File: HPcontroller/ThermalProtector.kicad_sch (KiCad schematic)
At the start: 5 parts

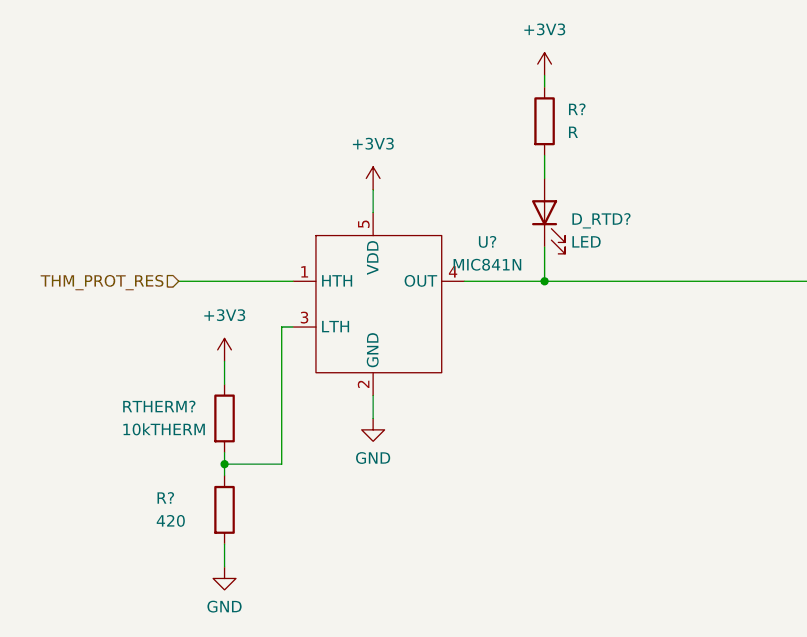
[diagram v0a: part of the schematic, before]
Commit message: assigned footprints, added some stuff to readme
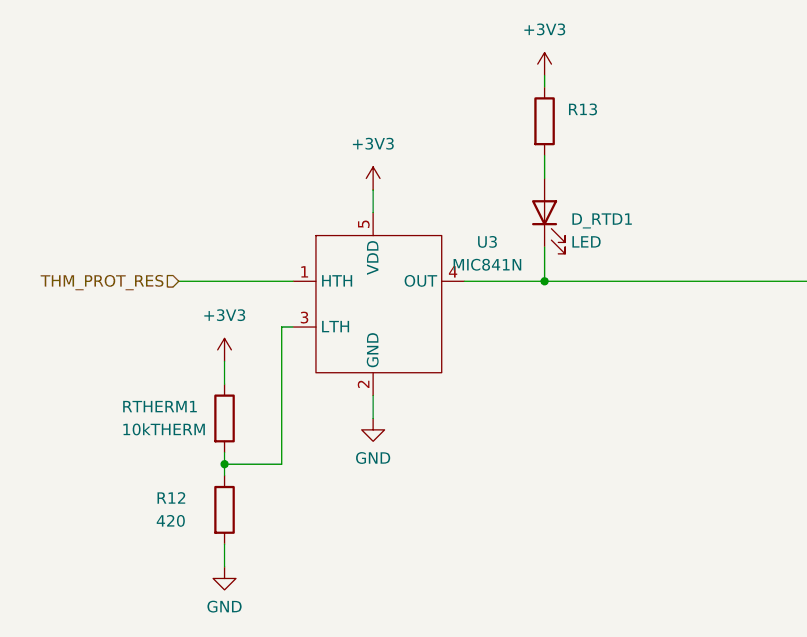
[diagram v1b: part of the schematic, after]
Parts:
- R13: renamed from R?; value R -> (none)
- gave numbers to parts that had none: 4
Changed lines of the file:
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@@
   (symbol (lib_id "Device:R") (at 114.3 104.14 0) (unit 1)
     (in_bom yes) (on_board yes)
-    (property "Reference" "RTHERM?" (id 0) (at 102.87 102.87 0)
+    (property "Reference" "RTHERM1" (id 0) (at 102.87 102.87 0)
       (effects (font (size 1.27 1.27)) (justify left))
     )
@@
   (symbol (lib_id "power:+3V3") (at 149.86 66.04 0) (unit 1)
     (in_bom yes) (on_board yes) (fields_autoplaced)
-    (property "Reference" "#PWR?" (id 0) (at 149.86 69.85 0)
+    (property "Reference" "#PWR0117" (id 0) (at 149.86 69.85 0)
       (effects (font (size 1.27 1.27)) hide)
     )
@@
   (symbol (lib_id "Device:R") (at 149.86 71.12 0) (unit 1)
     (in_bom yes) (on_board yes) (fields_autoplaced)
-    (property "Reference" "R?" (id 0) (at 152.4 69.8499 0)
+    (property "Reference" "R13" (id 0) (at 152.4 69.8499 0)
       (effects (font (size 1.27 1.27)) (justify left))
     )
-    (property "Value" "R" (id 1) (at 152.4 72.3899 0)
+    (property "Value" "" (id 1) (at 152.4 72.3899 0)
       (effects (font (size 1.27 1.27)) (justify left))
     )
@@
   (symbol (lib_id "Device:LED") (at 149.86 81.28 90) (unit 1)
     (in_bom yes) (on_board yes) (fields_autoplaced)
-    (property "Reference" "D_RTD?" (id 0) (at 152.781 82.0328 90)
+    (property "Reference" "D_RTD1" (id 0) (at 152.781 82.0328 90)
       (effects (font (size 1.27 1.27)) (justify right))
     )
@@
   (symbol (lib_id "power:+3V3") (at 114.3 97.79 0) (unit 1)
     (in_bom yes) (on_board yes) (fields_autoplaced)
-    (property "Reference" "#PWR?" (id 0) (at 114.3 101.6 0)
+    (property "Reference" "#PWR0115" (id 0) (at 114.3 101.6 0)
       (effects (font (size 1.27 1.27)) hide)
     )
@@
   (symbol (lib_id "power:GND") (at 130.81 104.14 0) (unit 1)
     (in_bom yes) (on_board yes) (fields_autoplaced)
-    (property "Reference" "#PWR?" (id 0) (at 130.81 110.49 0)
+    (property "Reference" "#PWR0118" (id 0) (at 130.81 110.49 0)
       (effects (font (size 1.27 1.27)) hide)
     )
@@
   (symbol (lib_id "power:GND") (at 114.3 120.65 0) (unit 1)
     (in_bom yes) (on_board yes) (fields_autoplaced)
-    (property "Reference" "#PWR?" (id 0) (at 114.3 127 0)
+    (property "Reference" "#PWR0114" (id 0) (at 114.3 127 0)
       (effects (font (size 1.27 1.27)) hide)
     )
@@
   (symbol (lib_id "HPsym:MIC841N") (at 130.81 91.44 0) (unit 1)
     (in_bom yes) (on_board yes) (fields_autoplaced)
-    (property "Reference" "U?" (id 0) (at 143.51 84.5693 0))
+    (property "Reference" "U3" (id 0) (at 143.51 84.5693 0))
     (property "Value" "MIC841N" (id 1) (at 143.51 87.1093 0))
     (property "Footprint" "" (id 2) (at 121.92 88.9 0)
@@
   (symbol (lib_id "power:+3V3") (at 130.81 78.74 0) (unit 1)
     (in_bom yes) (on_board yes) (fields_autoplaced)
-    (property "Reference" "#PWR?" (id 0) (at 130.81 82.55 0)
+    (property "Reference" "#PWR0116" (id 0) (at 130.81 82.55 0)
       (effects (font (size 1.27 1.27)) hide)
     )
@@
   (symbol (lib_id "Device:R") (at 114.3 114.3 0) (unit 1)
     (in_bom yes) (on_board yes)
-    (property "Reference" "R?" (id 0) (at 106.68 113.03 0)
+    (property "Reference" "R12" (id 0) (at 106.68 113.03 0)
       (effects (font (size 1.27 1.27)) (justify left))
     )

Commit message: started layout
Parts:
- added C5: C, symbol Device:C
- D_RTD1: footprint (none) -> LED_SMD:LED_0603_1608Metric_Pad1.05x0.95mm_HandSolder
- R12: footprint (none) -> Resistor_SMD:R_0805_2012Metric_Pad1.20x1.40mm_HandSolder
- R13: value (none) -> 100; footprint (none) -> Resistor_SMD:R_0805_2012Metric_Pad1.20x1.40mm_HandSolder
- U3: footprint (none) -> Package_TO_SOT_SMD:SOT-353_SC-70-5_Handsoldering
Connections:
- net +3V3: now also C5.1
- net GND: now also C5.2
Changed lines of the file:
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@@
   (junction (at 114.3 109.22) (diameter 0) (color 0 0 0 0)
   )
+  (junction (at 130.81 71.12) (diameter 0) (color 0 0 0 0)
+  )
   (wire (pts (xy 149.86 88.9) (xy 185.42 88.9))
     (stroke (width 0) (type default) (color 0 0 0 0))
@@
     (stroke (width 0) (type default) (color 0 0 0 0))
   )
+  (wire (pts (xy 116.84 73.66) (xy 116.84 71.12))
+    (stroke (width 0) (type default) (color 0 0 0 0))
+  )
   (wire (pts (xy 114.3 109.22) (xy 114.3 110.49))
     (stroke (width 0) (type default) (color 0 0 0 0))
@@
     (stroke (width 0) (type default) (color 0 0 0 0))
   )
-  (wire (pts (xy 130.81 78.74) (xy 130.81 81.28))
+  (wire (pts (xy 130.81 68.58) (xy 130.81 71.12))
     (stroke (width 0) (type default) (color 0 0 0 0))
   )
@@
     (stroke (width 0) (type default) (color 0 0 0 0))
   )
+  (wire (pts (xy 116.84 82.55) (xy 116.84 81.28))
+    (stroke (width 0) (type default) (color 0 0 0 0))
+  )
   (wire (pts (xy 149.86 88.9) (xy 140.97 88.9))
     (stroke (width 0) (type default) (color 0 0 0 0))
@@
     (stroke (width 0) (type default) (color 0 0 0 0))
   )
+  (wire (pts (xy 116.84 71.12) (xy 130.81 71.12))
+    (stroke (width 0) (type default) (color 0 0 0 0))
+  )
   (wire (pts (xy 120.65 109.22) (xy 114.3 109.22))
     (stroke (width 0) (type default) (color 0 0 0 0))
@@
   )
   (wire (pts (xy 114.3 118.11) (xy 114.3 120.65))
+    (stroke (width 0) (type default) (color 0 0 0 0))
+  )
+  (wire (pts (xy 130.81 71.12) (xy 130.81 81.28))
     (stroke (width 0) (type default) (color 0 0 0 0))
   )
@@
       (effects (font (size 1.27 1.27)) (justify left))
     )
-    (property "Value" "" (id 1) (at 152.4 72.3899 0)
-      (effects (font (size 1.27 1.27)) (justify left))
-    )
-    (property "Footprint" "" (id 2) (at 148.082 71.12 90)
+    (property "Value" "100" (id 1) (at 152.4 72.3899 0)
+      (effects (font (size 1.27 1.27)) (justify left))
+    )
+    (property "Footprint" "Resistor_SMD:R_0805_2012Metric_Pad1.20x1.40mm_HandSolder" (id 2) (at 148.082 71.12 90)
       (effects (font (size 1.27 1.27)) hide)
     )
@@
       (effects (font (size 1.27 1.27)) (justify right))
     )
-    (property "Footprint" "" (id 2) (at 149.86 81.28 0)
+    (property "Footprint" "LED_SMD:LED_0603_1608Metric_Pad1.05x0.95mm_HandSolder" (id 2) (at 149.86 81.28 0)
       (effects (font (size 1.27 1.27)) hide)
     )
@@
     (property "Reference" "U3" (id 0) (at 143.51 84.5693 0))
     (property "Value" "MIC841N" (id 1) (at 143.51 87.1093 0))
-    (property "Footprint" "" (id 2) (at 121.92 88.9 0)
+    (property "Footprint" "Package_TO_SOT_SMD:SOT-353_SC-70-5_Handsoldering" (id 2) (at 121.92 88.9 0)
       (effects (font (size 1.27 1.27)) hide)
     )
@@
     (pin "5")
   )
-  (symbol (lib_id "power:+3V3") (at 130.81 78.74 0) (unit 1)
-    (in_bom yes) (on_board yes) (fields_autoplaced)
-    (property "Reference" "#PWR0116" (id 0) (at 130.81 82.55 0)
-      (effects (font (size 1.27 1.27)) hide)
-    )
-    (property "Value" "+3V3" (id 1) (at 130.81 73.66 0))
-    (property "Footprint" "" (id 2) (at 130.81 78.74 0)
-      (effects (font (size 1.27 1.27)) hide)
-    )
-    (property "Datasheet" "" (id 3) (at 130.81 78.74 0)
+  (symbol (lib_id "Device:C") (at 116.84 77.47 0) (unit 1)
+    (in_bom yes) (on_board yes) (fields_autoplaced)
+    (property "Reference" "C5" (id 0) (at 119.761 76.6353 0)
+      (effects (font (size 1.27 1.27)) (justify left))
+    )
+    (property "Value" "C" (id 1) (at 119.761 79.1722 0)
+      (effects (font (size 1.27 1.27)) (justify left))
+    )
+    (property "Footprint" "" (id 2) (at 117.8052 81.28 0)
+      (effects (font (size 1.27 1.27)) hide)
+    )
+    (property "Datasheet" "~" (id 3) (at 116.84 77.47 0)
+      (effects (font (size 1.27 1.27)) hide)
+    )
+    (pin "1")
+    (pin "2")
+  )
+  (symbol (lib_id "power:GND") (at 116.84 82.55 0) (unit 1)
+    (in_bom yes) (on_board yes) (fields_autoplaced)
+    (property "Reference" "#PWR0135" (id 0) (at 116.84 88.9 0)
+      (effects (font (size 1.27 1.27)) hide)
+    )
+    (property "Value" "GND" (id 1) (at 116.84 86.9934 0))
+    (property "Footprint" "" (id 2) (at 116.84 82.55 0)
+      (effects (font (size 1.27 1.27)) hide)
+    )
+    (property "Datasheet" "" (id 3) (at 116.84 82.55 0)
+      (effects (font (size 1.27 1.27)) hide)
+    )
+    (pin "1")
+  )
+  (symbol (lib_id "power:+3V3") (at 130.81 68.58 0) (unit 1)
+    (in_bom yes) (on_board yes) (fields_autoplaced)
+    (property "Reference" "#PWR0116" (id 0) (at 130.81 72.39 0)
+      (effects (font (size 1.27 1.27)) hide)
+    )
+    (property "Value" "+3V3" (id 1) (at 130.81 63.5 0))
+    (property "Footprint" "" (id 2) (at 130.81 68.58 0)
+      (effects (font (size 1.27 1.27)) hide)
+    )
+    (property "Datasheet" "" (id 3) (at 130.81 68.58 0)
       (effects (font (size 1.27 1.27)) hide)
     )
@@
       (effects (font (size 1.27 1.27)) (justify left))
     )
-    (property "Footprint" "" (id 2) (at 112.522 114.3 90)
-      (effects (font (size 1.27 1.27)) hide)
-    )
+    (property "Footprint" "Resistor_SMD:R_0805_2012Metric_Pad1.20x1.40mm_HandSolder" (id 2) (at 112.522 114.3 90)
+      (effects (font (size 1.27 1.27)) hide)
+    )

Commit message: routing more.  waitingfor PD trigger to arrive
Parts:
- C5: footprint (none) -> Capacitor_SMD:C_0805_2012Metric_Pad1.18x1.45mm_HandSolder
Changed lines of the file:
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@@
       (effects (font (size 1.27 1.27)) (justify left))
     )
-    (property "Footprint" "" (id 2) (at 117.8052 81.28 0)
+    (property "Footprint" "Capacitor_SMD:C_0805_2012Metric_Pad1.18x1.45mm_HandSolder" (id 2) (at 117.8052 81.28 0)
       (effects (font (size 1.27 1.27)) hide)
     )

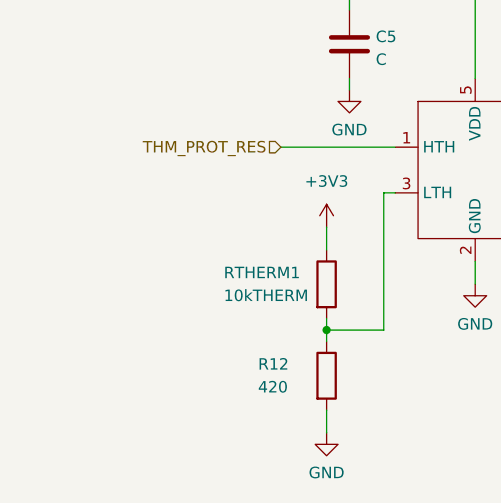
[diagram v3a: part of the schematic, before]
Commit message: minor pcb change to give TC wires more room
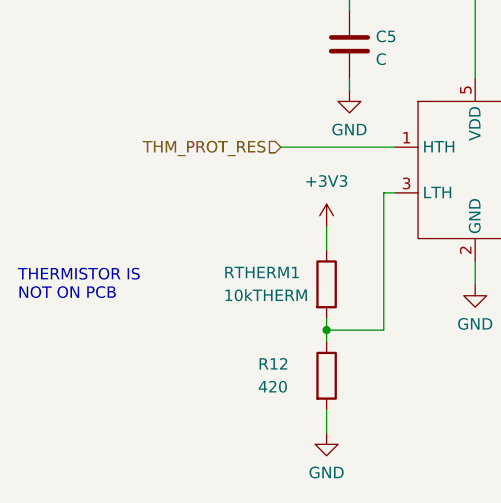
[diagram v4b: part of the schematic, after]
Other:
- note added: "THERMISTOR IS NOT ON PCB"
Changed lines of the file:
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@@
     (stroke (width 0) (type default) (color 0 0 0 0))
+  )
+  (text "THERMISTOR IS\nNOT ON PCB" (at 80.01 106.045 0)
+    (effects (font (size 1.27 1.27)) (justify left bottom))
   )
   (hierarchical_label "THM_PROT_OUT" (shape input) (at 185.42 88.9 0)

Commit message: fixed minor issues, added mounting
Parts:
- RTHERM1: footprint (none) -> Resistor_SMD:R_0805_2012Metric_Pad1.20x1.40mm_HandSolder
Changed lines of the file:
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@@
       (effects (font (size 1.27 1.27)) (justify left))
     )
-    (property "Footprint" "" (id 2) (at 112.522 104.14 90)
+    (property "Footprint" "Resistor_SMD:R_0805_2012Metric_Pad1.20x1.40mm_HandSolder" (id 2) (at 112.522 104.14 90)
       (effects (font (size 1.27 1.27)) hide)
     )

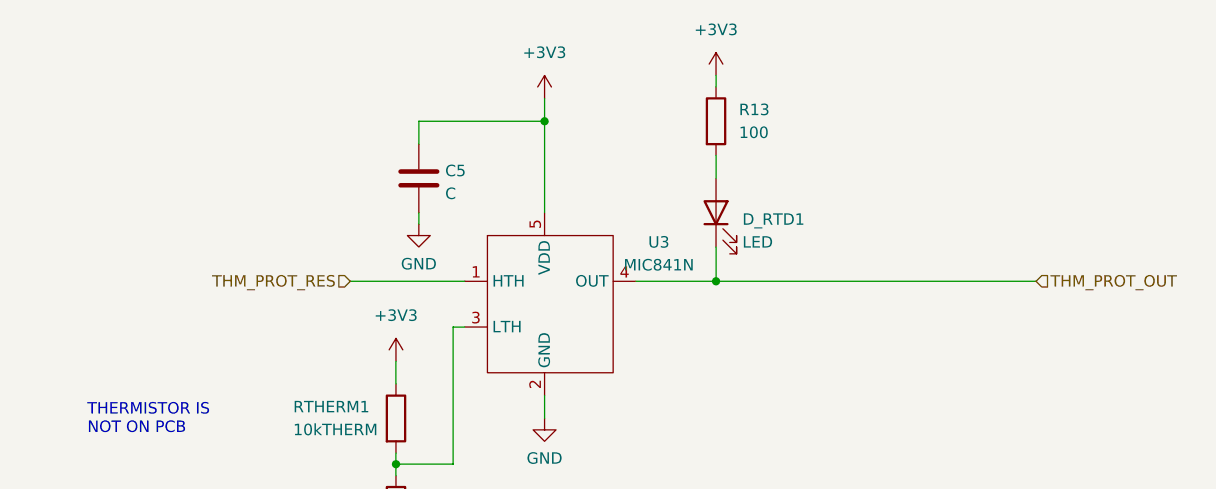
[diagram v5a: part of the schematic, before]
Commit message: added upllup to thermal protection circuit
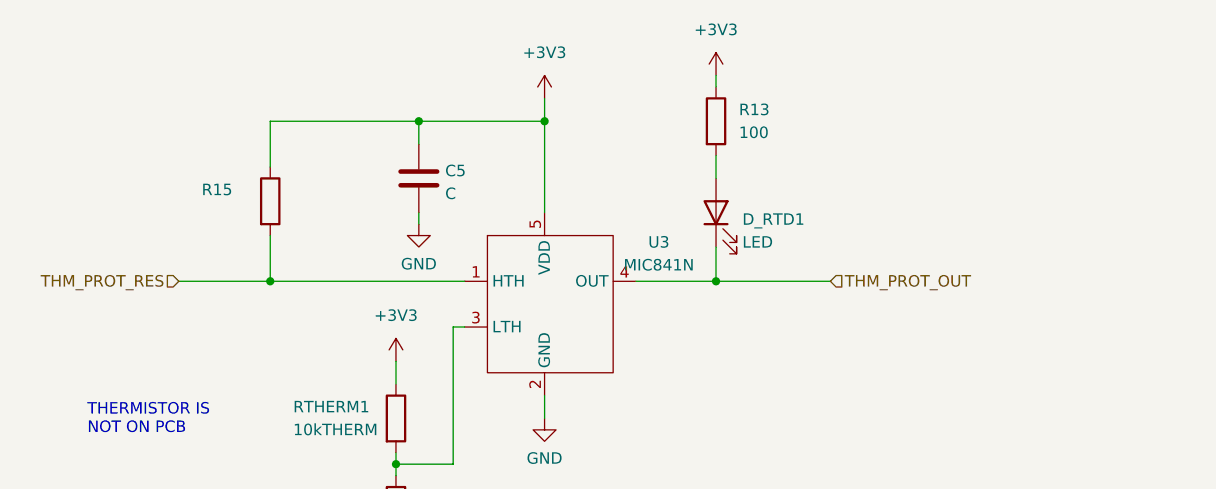
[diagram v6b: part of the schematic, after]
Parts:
- added R15: (no value), Resistor_SMD:R_0805_2012Metric_Pad1.20x1.40mm_HandSolder, symbol Device:R
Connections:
- net +3V3: now also R15.1
- net THM_PROT_RES: now also R15.2
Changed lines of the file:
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@@
 (kicad_sch (version 20211123) (generator eeschema)
   (paper "A4")
+  (junction (at 116.84 71.12) (diameter 0) (color 0 0 0 0)
+  )
   (junction (at 149.86 88.9) (diameter 0) (color 0 0 0 0)
   )
@@
   (junction (at 130.81 71.12) (diameter 0) (color 0 0 0 0)
   )
-  (wire (pts (xy 149.86 88.9) (xy 185.42 88.9))
+  (junction (at 100.33 88.9) (diameter 0) (color 0 0 0 0)
+  )
+  (wire (pts (xy 149.86 88.9) (xy 162.56 88.9))
     (stroke (width 0) (type default) (color 0 0 0 0))
   )
@@
     (stroke (width 0) (type default) (color 0 0 0 0))
   )
+  (wire (pts (xy 100.33 71.12) (xy 116.84 71.12))
+    (stroke (width 0) (type default) (color 0 0 0 0))
+  )
+  (wire (pts (xy 100.33 76.2) (xy 100.33 71.12))
+    (stroke (width 0) (type default) (color 0 0 0 0))
+  )
   (wire (pts (xy 116.84 73.66) (xy 116.84 71.12))
     (stroke (width 0) (type default) (color 0 0 0 0))
@@
     (stroke (width 0) (type default) (color 0 0 0 0))
   )
+  (wire (pts (xy 100.33 83.82) (xy 100.33 88.9))
+    (stroke (width 0) (type default) (color 0 0 0 0))
+  )
   (wire (pts (xy 114.3 109.22) (xy 114.3 107.95))
     (stroke (width 0) (type default) (color 0 0 0 0))
@@
     (stroke (width 0) (type default) (color 0 0 0 0))
   )
-  (wire (pts (xy 109.22 88.9) (xy 121.92 88.9))
+  (wire (pts (xy 90.17 88.9) (xy 100.33 88.9))
     (stroke (width 0) (type default) (color 0 0 0 0))
   )
@@
   )
   (wire (pts (xy 120.65 93.98) (xy 120.65 109.22))
+    (stroke (width 0) (type default) (color 0 0 0 0))
+  )
+  (wire (pts (xy 100.33 88.9) (xy 121.92 88.9))
     (stroke (width 0) (type default) (color 0 0 0 0))
   )
@@
     (effects (font (size 1.27 1.27)) (justify left bottom))
   )
-  (hierarchical_label "THM_PROT_OUT" (shape input) (at 185.42 88.9 0)
+  (hierarchical_label "THM_PROT_OUT" (shape input) (at 162.56 88.9 0)
     (effects (font (size 1.27 1.27)) (justify left))
   )
-  (hierarchical_label "THM_PROT_RES" (shape input) (at 109.22 88.9 180)
+  (hierarchical_label "THM_PROT_RES" (shape input) (at 90.17 88.9 180)
     (effects (font (size 1.27 1.27)) (justify right))
   )
@@
       (effects (font (size 1.27 1.27)) hide)
     )
+    (pin "1")
+    (pin "2")
+  )
+  (symbol (lib_id "Device:R") (at 100.33 80.01 0) (unit 1)
+    (in_bom yes) (on_board yes)
+    (property "Reference" "R15" (id 0) (at 92.71 78.74 0)
+      (effects (font (size 1.27 1.27)) (justify left))
+    )
+    (property "Value" "" (id 1) (at 92.71 81.28 0)
+      (effects (font (size 1.27 1.27)) (justify left))
+    )
+    (property "Footprint" "Resistor_SMD:R_0805_2012Metric_Pad1.20x1.40mm_HandSolder" (id 2) (at 98.552 80.01 90)
+      (effects (font (size 1.27 1.27)) hide)
+    )
+    (property "Datasheet" "~" (id 3) (at 100.33 80.01 0)
+      (effects (font (size 1.27 1.27)) hide)
+    )

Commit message: started revision
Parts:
- R15: value (none) -> 10k
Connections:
- net THM_PROT_RES: now also U3.3 (LTH); no longer U3.1 (HTH)
- net at R12.1, RTHERM1.2: now also U3.1 (HTH); no longer U3.3 (LTH)
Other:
- moved on the sheet: R12, RTHERM1
